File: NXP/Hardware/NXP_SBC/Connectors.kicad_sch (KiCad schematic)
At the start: 13 parts, among them J2 54104-4031, J3 52271-0679, J4 RJ45_Wuerth_7499010121A, J5 USB_A

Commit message: Added some more to the DDR memory schematic
Upgraded the project to kicad 9.0
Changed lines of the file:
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@@
 (kicad_sch
-	(version 20231120)
+	(version 20250114)
 	(generator "eeschema")
-	(generator_version "8.0")
+	(generator_version "9.0")
 	(paper "A3")

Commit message: minor updates
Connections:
- no-connect marks 0 -> 4

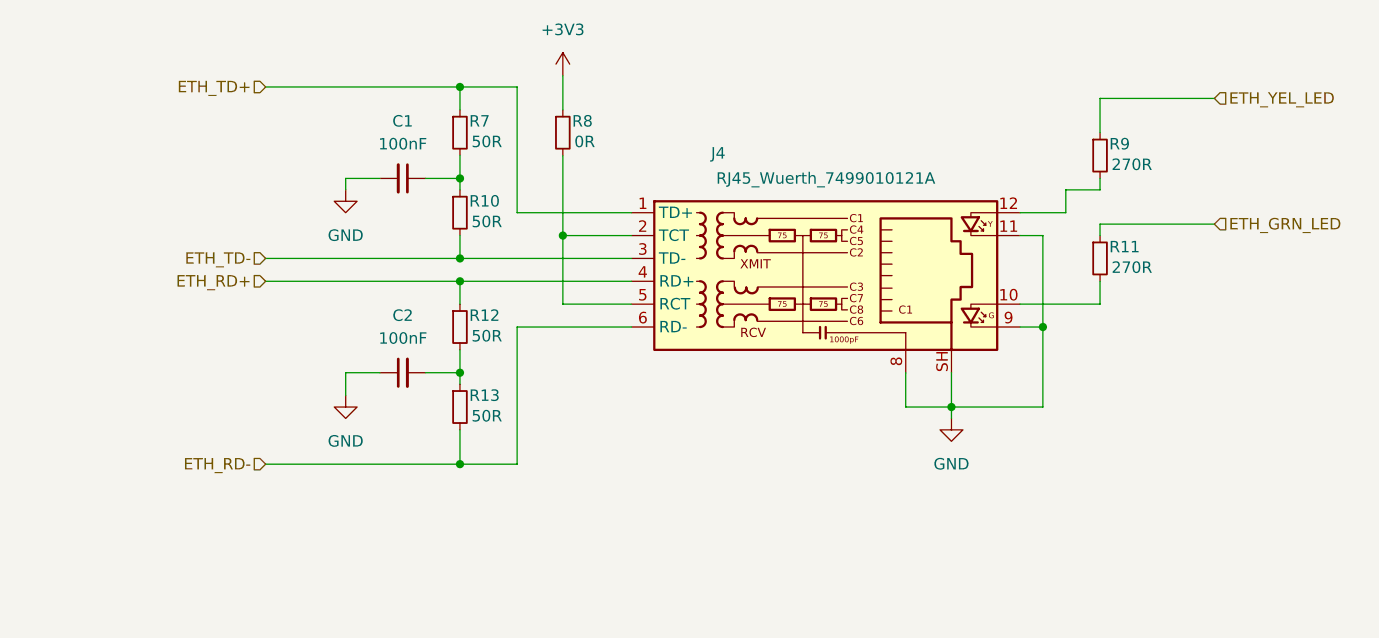
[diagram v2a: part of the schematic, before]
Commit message: Added more to ethernet schematic
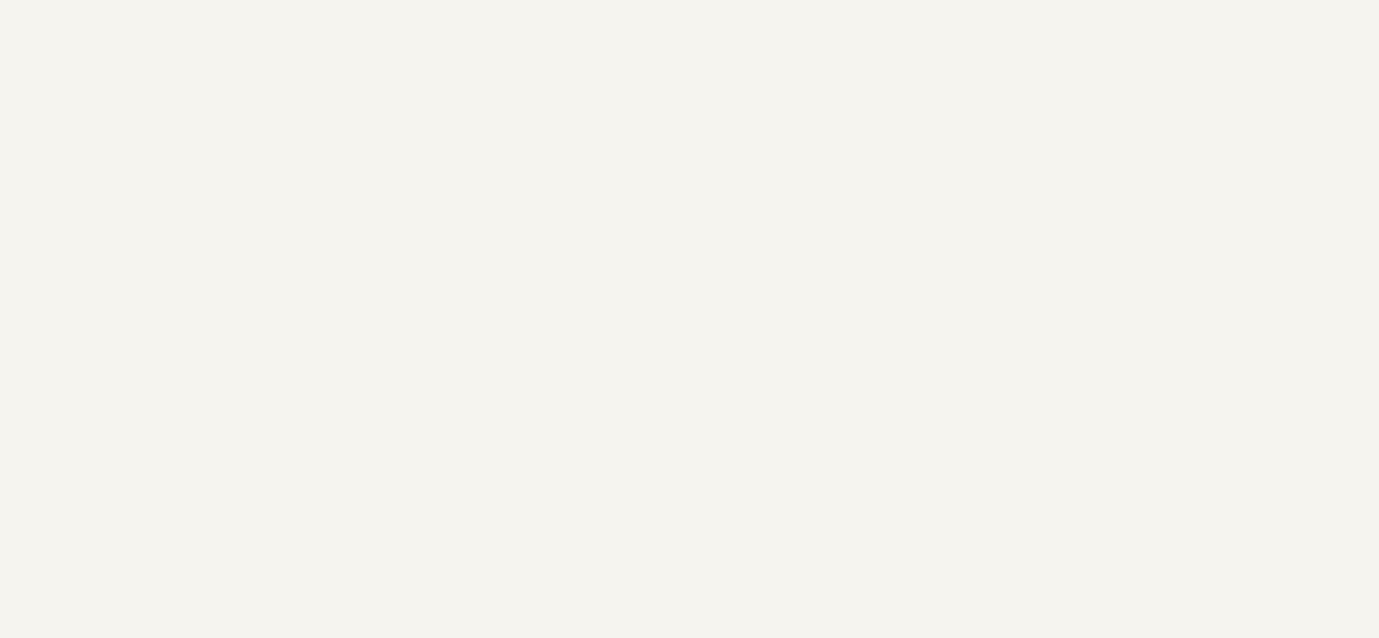
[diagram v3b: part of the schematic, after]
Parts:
- removed C1, C2: 100nF, Capacitor_SMD:C_0603_1608Metric_Pad1.08x0.95mm_HandSolder, symbol Device:C_Small
- removed J4: RJ45_Wuerth_7499010121A, Connector_RJ:RJ45_Wuerth_7499010121A_Horizontal, symbol Connector:RJ45_Wuerth_7499010121A
- removed R10, R12, R13, R7: 50R, Resistor_SMD:R_01005_0402Metric, symbol Device:R_Small
- removed R11, R9: 270R, Resistor_SMD:R_01005_0402Metric, symbol Device:R_Small
- removed R8: 0R, Resistor_SMD:R_01005_0402Metric, symbol Device:R_Small

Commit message: More updates to schematic
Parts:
- added R74: 10K, 1%, Resistor_SMD:R_0603_1608Metric, symbol Device:R_Small
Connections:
- net GND: now also R74.1
- net LCD_BIST: now also R74.2
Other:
- note added: "Backlight = 50mA LCD = 240mA"
- moved on the sheet: J3
